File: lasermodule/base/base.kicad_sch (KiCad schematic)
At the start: 5 parts, among them J1 Connector_Generic_Conn_01x02, J2 FPC 15 pin molex vertical, U10 MCP1700x-330xxTT, U9 LM7805_TO220

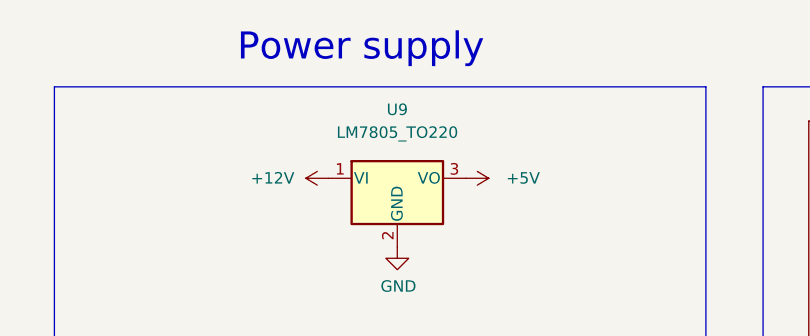
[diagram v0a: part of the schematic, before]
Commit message: added pcbmotor, renamed some folders
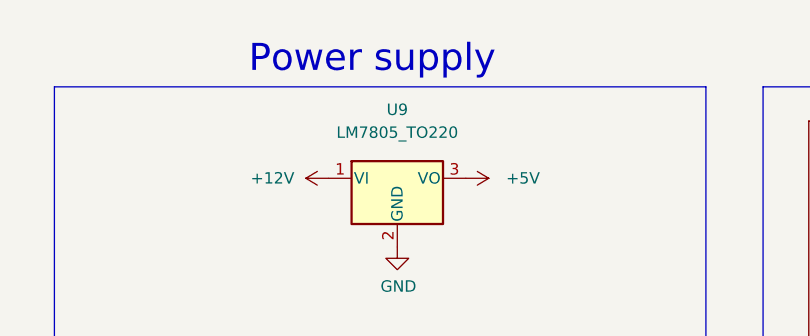
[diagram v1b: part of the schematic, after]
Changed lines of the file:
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@@
     (stroke (width 0) (type default))
   )
-  (text "Power supply" (at 113.03 40.64 0)
+  (text "Power supply" (at 114.3 41.91 0)
     (effects (font (size 3 3)) (justify left bottom))
   )

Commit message: further cleaned up and tested renders in blender
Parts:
- J1: footprint Connector_AMASS:AMASS_XT30PW-F_1x02_P2.50mm_Horizontal -> sockets_scanhead:AMASS_XT30PW-F_1x02_P2.50mm_Horizontal
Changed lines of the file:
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@@
     (pin "1")
     (instances
-      (project "scanhead_pcb"
+      (project "base"
         (path "/e63e39d7-6ac0-4ffd-8aa3-1841a4541b55"
           (reference "#PWR05") (unit 1)
@@
     (pin "1")
     (instances
-      (project "scanhead_pcb"
+      (project "base"
         (path "/e63e39d7-6ac0-4ffd-8aa3-1841a4541b55"
           (reference "#FLG03") (unit 1)
@@
     (pin "1")
     (instances
-      (project "scanhead_pcb"
+      (project "base"
         (path "/e63e39d7-6ac0-4ffd-8aa3-1841a4541b55"
           (reference "#FLG02") (unit 1)
@@
     (pin "1")
     (instances
-      (project "scanhead_pcb"
+      (project "base"
         (path "/e63e39d7-6ac0-4ffd-8aa3-1841a4541b55"
           (reference "#PWR03") (unit 1)
@@
     (pin "9_1")
     (instances
-      (project "scanhead_pcb"
+      (project "base"
         (path "/e63e39d7-6ac0-4ffd-8aa3-1841a4541b55"
           (reference "J2") (unit 1)
@@
     (pin "2")
     (instances
-      (project "scanhead_pcb"
+      (project "base"
         (path "/e63e39d7-6ac0-4ffd-8aa3-1841a4541b55"
           (reference "F3") (unit 1)
@@
     (pin "1")
     (instances
-      (project "scanhead_pcb"
+      (project "base"
         (path "/e63e39d7-6ac0-4ffd-8aa3-1841a4541b55"
           (reference "#PWR018") (unit 1)
@@
     (pin "3")
     (instances
-      (project "scanhead_pcb"
+      (project "base"
         (path "/e63e39d7-6ac0-4ffd-8aa3-1841a4541b55"
           (reference "U10") (unit 1)
@@
     (pin "1")
     (instances
-      (project "scanhead_pcb"
+      (project "base"
         (path "/e63e39d7-6ac0-4ffd-8aa3-1841a4541b55"
           (reference "#PWR04") (unit 1)
@@
     (pin "1")
     (instances
-      (project "scanhead_pcb"
+      (project "base"
         (path "/e63e39d7-6ac0-4ffd-8aa3-1841a4541b55"
           (reference "#PWR013") (unit 1)
@@
     (pin "1")
     (instances
-      (project "scanhead_pcb"
+      (project "base"
         (path "/e63e39d7-6ac0-4ffd-8aa3-1841a4541b55"
           (reference "#PWR015") (unit 1)
@@
     (pin "1")
     (instances
-      (project "scanhead_pcb"
+      (project "base"
         (path "/e63e39d7-6ac0-4ffd-8aa3-1841a4541b55"
           (reference "#PWR06") (unit 1)
@@
     (pin "1")
     (instances
-      (project "scanhead_pcb"
+      (project "base"
         (path "/e63e39d7-6ac0-4ffd-8aa3-1841a4541b55"
           (reference "#PWR016") (unit 1)
@@
       (effects (font (size 1.27 1.27)))
     )
-    (property "Footprint" "Connector_AMASS:AMASS_XT30PW-F_1x02_P2.50mm_Horizontal" (at 55.88 62.23 0)
+    (property "Footprint" "sockets_scanhead:AMASS_XT30PW-F_1x02_P2.50mm_Horizontal" (at 55.88 62.23 0)
       (effects (font (size 1.27 1.27)) hide)
     )
@@
     (pin "2")
     (instances
-      (project "scanhead_pcb"
+      (project "base"
         (path "/e63e39d7-6ac0-4ffd-8aa3-1841a4541b55"
           (reference "J1") (unit 1)
@@
     (pin "3")
     (instances
-      (project "scanhead_pcb"
+      (project "base"
         (path "/e63e39d7-6ac0-4ffd-8aa3-1841a4541b55"
           (reference "U9") (unit 1)
@@
     (pin "1")
     (instances
-      (project "scanhead_pcb"
+      (project "base"
         (path "/e63e39d7-6ac0-4ffd-8aa3-1841a4541b55"
           (reference "#PWR019") (unit 1)
@@
     )
     (instances
-      (project "scanhead_pcb"
+      (project "base"
         (path "/e63e39d7-6ac0-4ffd-8aa3-1841a4541b55" (page "3"))
       )
@@
     )
     (instances
-      (project "scanhead_pcb"
+      (project "base"
         (path "/e63e39d7-6ac0-4ffd-8aa3-1841a4541b55" (page "2"))
       )
